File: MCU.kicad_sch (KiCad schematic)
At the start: 16 parts, among them J2 FTDI, SW1 SW_MEC_5G, SW2 SW_MEC_5G, U1 ESP32-WROOM-32, U2 AMS1117-3.3

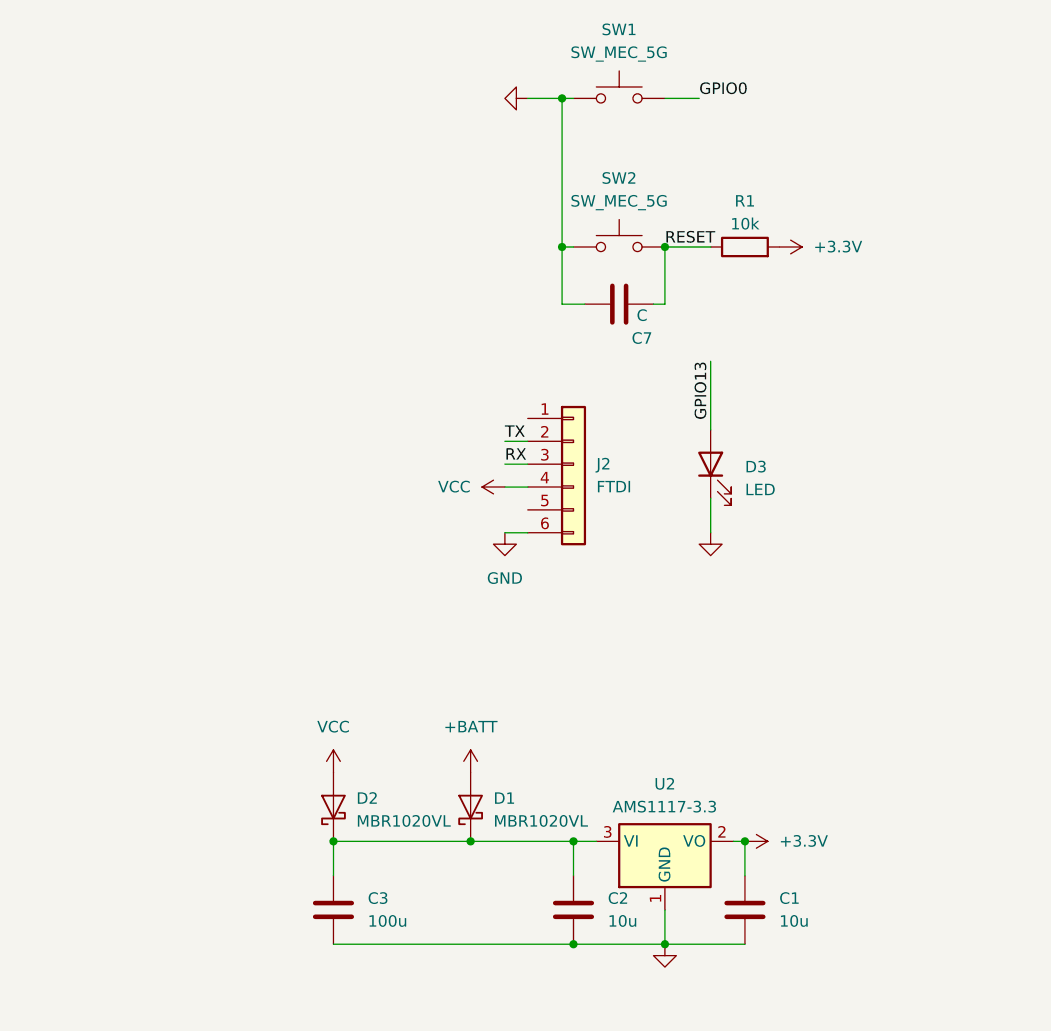
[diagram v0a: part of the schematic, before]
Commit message: Power Section done + added backup lipo
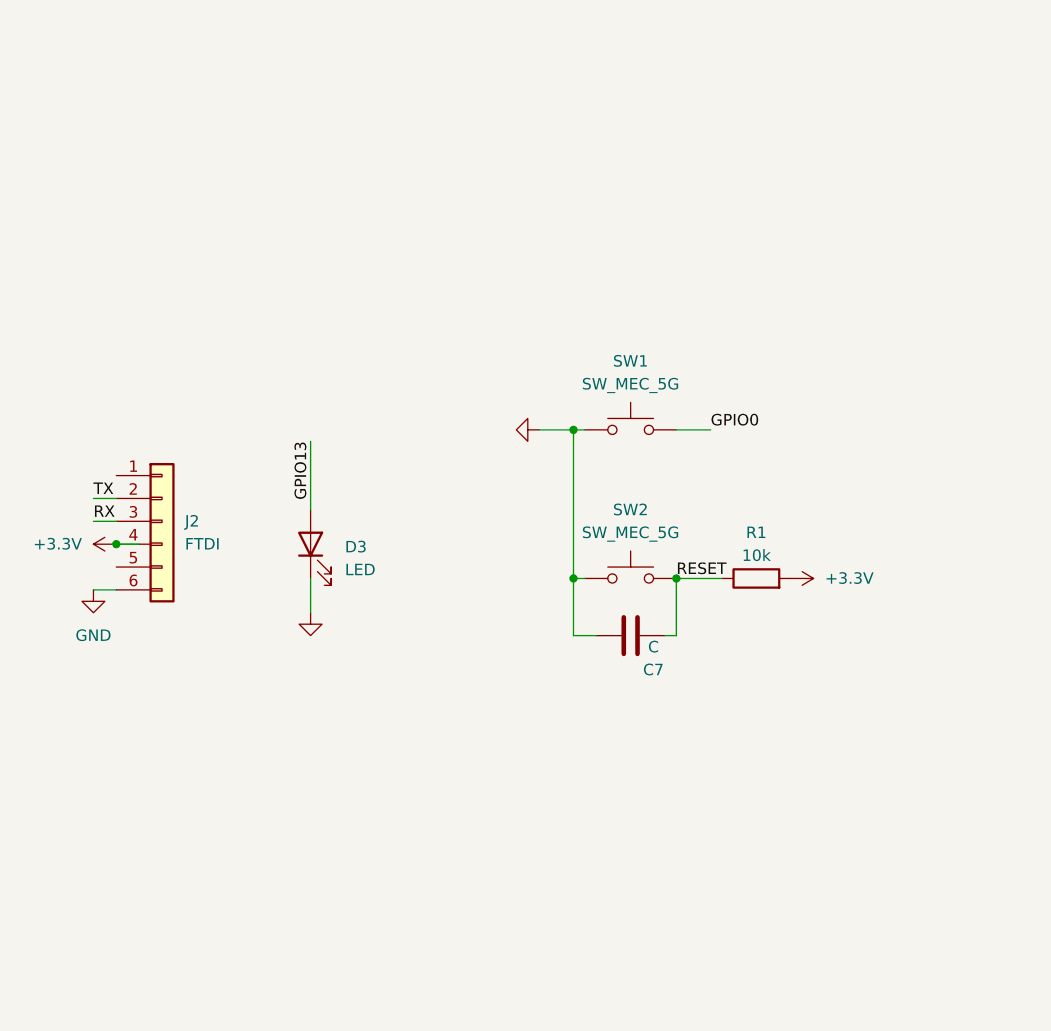
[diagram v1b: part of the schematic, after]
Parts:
- removed C1, C2: 10u, symbol Device:C
- removed C3: 100u, symbol Device:C
- removed D1, D2: MBR1020VL, Diode_SMD:D_SOD-123F, symbol Diode:MBR1020VL
- removed U2: AMS1117-3.3, Package_TO_SOT_SMD:SOT-223-3_TabPin2, symbol Regulator_Linear:AMS1117-3.3
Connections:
- net VCC is gone; now on net +3.3V: J2.4 (Pin_4)
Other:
- moved on the sheet: C7, D3, J2, R1, SW1, SW2

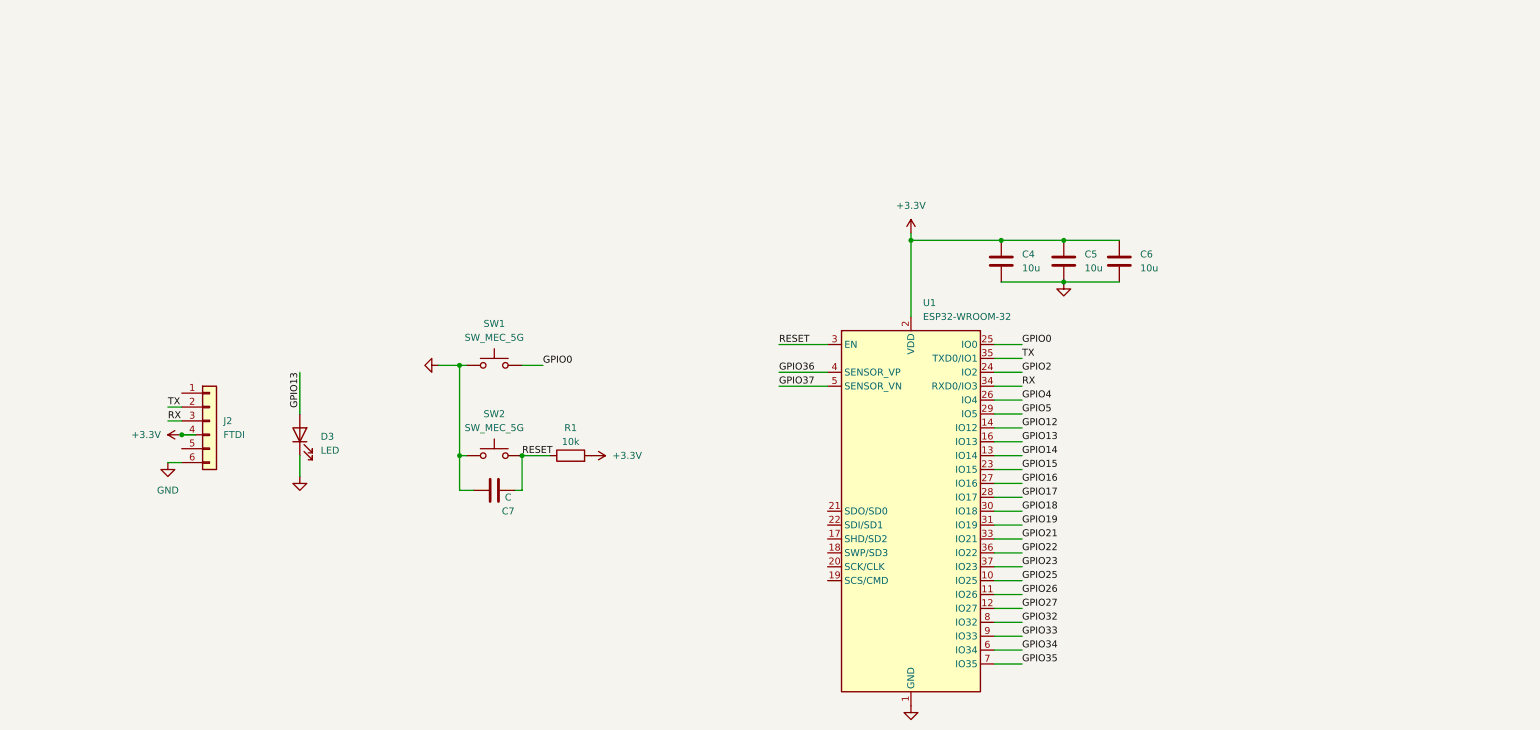
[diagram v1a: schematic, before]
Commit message: added io expander + rtc + fuel guage
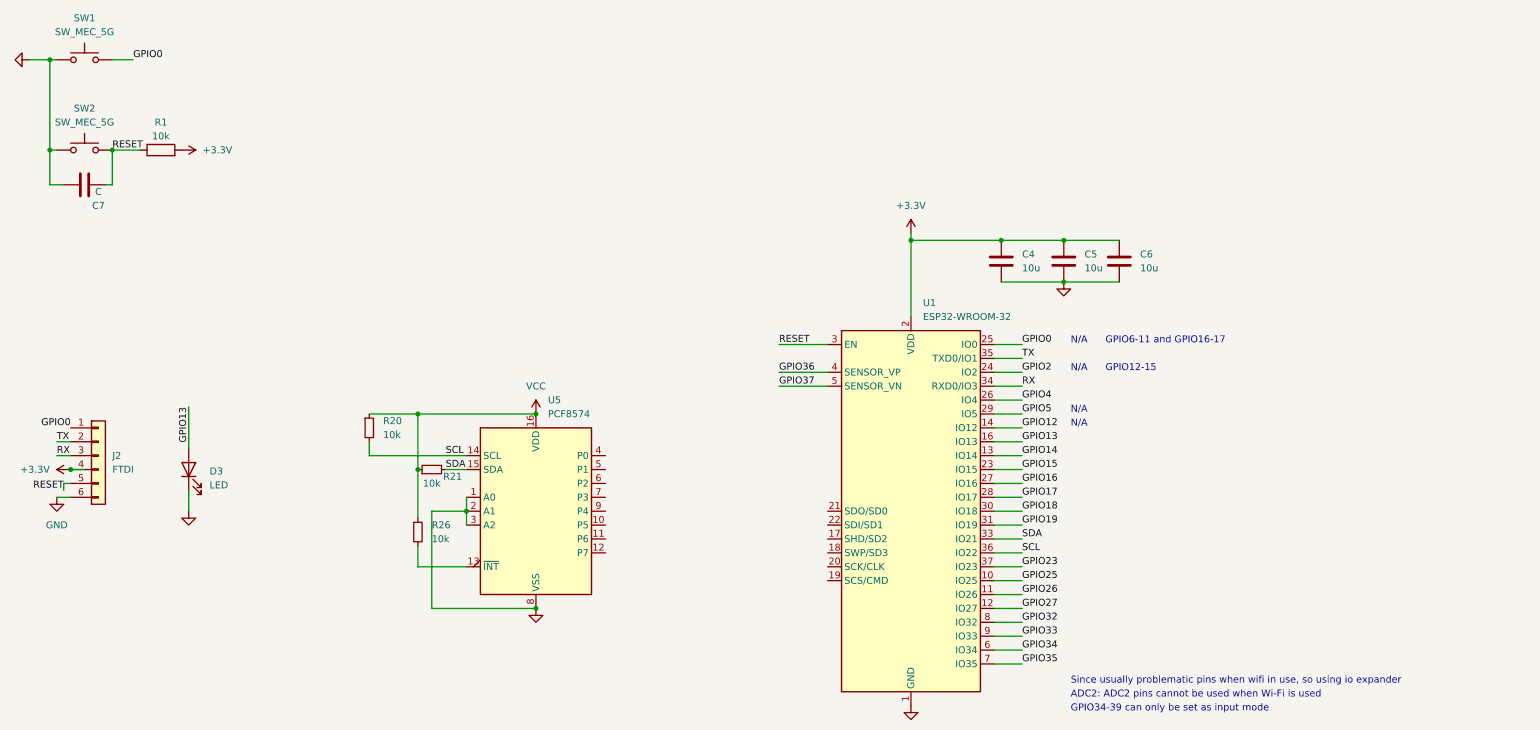
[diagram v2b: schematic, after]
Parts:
- added R20, R21, R26: 10k, symbol Device:R_Small
- added U5: PCF8574, symbol Interface_Expansion:PCF8574
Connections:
- net GND: now also U5.1 (A0), U5.2 (A1), U5.3 (A2), U5.8 (VSS)
- net GPIO0: now also J2.1 (Pin_1)
- net RESET: now also J2.5 (Pin_5)
- net GPIO21 renamed SDA
- net SDA: now also R21.2, U5.15 (SDA)
- net GPIO22 renamed SCL
- net SCL: now also R20.2, U5.14 (SCL)
- new net: R26.2, U5.13 (~{INT})
- new net VCC: R20.1, R21.1, R26.1, U5.16 (VDD)
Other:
- note added: "ADC2: ADC2 pins cannot be used when Wi-Fi is used"
- note added: "GPIO12-15"
- note added: "GPIO34-39 can only be set as input mode"
- note added: "GPIO6-11 and GPIO16-17"
- note added: "N/A"
- note added: "Since usually problematic pins when wifi in use, so using io expander"
- moved on the sheet: C7, D3, J2, R1, SW1, SW2

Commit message: Schematic Completed
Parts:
- removed D3: LED, symbol Device:LED
- added BT1: CR1220, symbol Device:Battery_Cell
- added C10: 10U, symbol Device:C
- added C11, C12: 6p, symbol Device:C_Small
- added C4: C_Small, symbol Device:C_Small
- added C9: 0.1U, symbol Device:C
- added R3, R4: 10k, symbol Device:R
- added R33, R34: 10k, symbol Device:R_Small
- added U3: DS3231M, Package_SO:SOIC-16W_7.5x10.3mm_P1.27mm, symbol Timer_RTC:DS3231M
- added U8: DS1307+, Package_DIP:DIP-8_W7.62mm, symbol Timer_RTC:DS1307+
- added Y1: 32.768kHz Quartz Crystal, symbol Device:Crystal_Small
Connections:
- net +3.3V: now also C10.1, C9.1, R3.1, R4.1, U3.2 (VCC)
- net GND: now also BT1.2 (-), C10.2, C4.1, C9.2, U3.10 (GND), U3.11 (GND), U3.12 (GND), U3.13 (GND), U3.5 (GND), U3.6 (GND), U3.7 (GND), U3.8 (GND), U3.9 (GND), U8.4 (GND)
- net SCL: now also R33.2, R4.2, U3.16 (SCL), U8.6 (SCL)
- net SDA: now also R3.2, R34.2, U3.15 (SDA), U8.5 (SDA)
- net VCC: now also C4.2, R33.1, R34.1, U8.3 (VBAT), U8.8 (VCC)
- net P_IO_4: now reaches U5.10 (P5)
- net P_IO_4: now also U5.9 (P4)
- net P_IO_5: now reaches U5.11 (P6)
- net P_IO_6: now reaches U5.12 (P7)
- net FAULT_LED: now reaches U5.4 (P0)
- net BUSY_LED: now reaches U5.5 (P1)
- net CON_LED: now reaches U5.6 (P2)
- net LED_PIN: now reaches U5.7 (P3)
- net GPIO13 renamed IO_LED
- net GPIO14 renamed MIST_PIN
- net GPIO15 renamed 12V_status
- net GPIO18 renamed TEMP1_DATA
- net GPIO19 renamed TEMP2_DATA
- net GPIO23 renamed BUZ_PIN
- net GPIO25 renamed WATER_PUMP_PIN
- net GPIO26 renamed FAN_EXHAUST_PIN
- net GPIO27 renamed turner
- net GPIO32 renamed heater
- net GPIO33 renamed ROTARY_DATA
- net GPIO34 renamed ROTARY_CLK
- net GPIO35 renamed ROT_SW
- net GPIO4 renamed FAN_CON_PIN
- net GPIO5 renamed WATER_LEVEL_DATA
- new net: BT1.1 (+), U3.14 (VBAT)
- new net: C11.1, C12.1
- new net: C12.2, U8.1 (X1), Y1.2
- new net: C11.2, U8.2 (X2), Y1.1
- new net 32KHZ: U3.1 (32KHZ)
- new net RTC_RESET: U3.4 (~{RST})
- new net SQW: U3.3 (~{INT}/SQW)
- no-connect marks 0 -> 6
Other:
- note added: "IE/OD"
- note added: "IO EXPANDER"
- note added: "MCU"
- note added: "OPTIONAL"
- note added: "PRIMARY"
- note added: "RTC"
- moved on the sheet: C4, C5, C6, C7, J2, R1, R20, R21, R26, SW1, SW2, U1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

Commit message: assigned footprints. another look needed. moving to pcb
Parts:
- removed BT1: CR1220, symbol Device:Battery_Cell
- removed C10: 10U, symbol Device:C
- removed C9: 0.1U, symbol Device:C
- removed R3, R4: 10k, symbol Device:R
- removed U3: DS3231M, Package_SO:SOIC-16W_7.5x10.3mm_P1.27mm, symbol Timer_RTC:DS3231M
- added BZ1: Buzzer, Buzzer_Beeper:Buzzer_12x9.5RM7.6, symbol Device:Buzzer
- added C1, C14: 0.1u, Capacitor_SMD:C_0402_1005Metric, symbol Device:C_Small
- added C13, C15, C17, C2, C8: 10u, Capacitor_SMD:C_0402_1005Metric, symbol Device:C_Small
- added C16: 10u, Capacitor_SMD:C_0805_2012Metric, symbol Device:C_Small
- added C18, C19, C21: 22u, Capacitor_SMD:C_0402_1005Metric, symbol Device:C_Small
- added C20: 10u, Capacitor_SMD:C_0402_1005Metric, symbol Device:C
- added D10, D11, D3, D6, D8: 1N4001, Diode_SMD:D_0805_2012Metric, symbol Diode:1N4001
- added D12: 1N5819, Diode_SMD:D_0805_2012Metric, symbol Diode:1N5819
- added D13, D14, D3: LED, LED_SMD:LED_0805_2012Metric, symbol Device:LED
- added D2: LED_PWR, LED_SMD:LED_0805_2012Metric, symbol Device:LED
- added D4: FAULT_LED, LED_SMD:LED_0805_2012Metric, symbol Device:LED
- added D5: BUSY_LED, Diode_SMD:D_0805_2012Metric, symbol Device:LED
- added D7: CONNECTIVITY_LED, LED_SMD:LED_0805_2012Metric, symbol Device:LED
- added F1: CAR_FUSE 2A, Fuse:Fuse_1206_3216Metric, symbol Device:Fuse
- added J10: mist, Connector_JST:JST_GH_SM02B-GHS-TB_1x02-1MP_P1.25mm_Horizontal, symbol Connector_Generic:Conn_01x02
- added J11: Led, LED_SMD:LED_0805_2012Metric, symbol Connector_Generic:Conn_01x02
- added J12: Water_Level, Connector_JST:JST_GH_SM03B-GHS-TB_1x03-1MP_P1.25mm_Horizontal, symbol Connector_Generic:Conn_01x03
- added J13: Main_Input_Jack, Connector_BarrelJack:BarrelJack_CLIFF_FC681465S_SMT_Horizontal, symbol Connector:Jack-DC
- added J14: Battery, Connector_JST:JST_EH_B2B-EH-A_1x02_P2.50mm_Vertical, symbol PCM_SL_Connectors:JST_02
- added J15: Display, Connector_JST:JST_GH_SM04B-GHS-TB_1x04-1MP_P1.25mm_Horizontal, symbol Connector_Generic:Conn_01x04
- added J16: Rotary_Encoder, Connector_JST:JST_GH_SM03B-GHS-TB_1x03-1MP_P1.25mm_Horizontal, symbol Connector_Generic:Conn_01x05
- added J17: Temp, Connector_JST:JST_GH_SM03B-GHS-TB_1x03-1MP_P1.25mm_Horizontal, symbol Connector_Generic:Conn_01x03
- added J18: Temp2, Connector_JST:JST_GH_SM03B-GHS-TB_1x03-1MP_P1.25mm_Horizontal, symbol Connector_Generic:Conn_01x03
- added J19: Water_Pump, Connector_JST:JST_GH_SM02B-GHS-TB_1x02-1MP_P1.25mm_Horizontal, symbol Connector_Generic:Conn_01x02
- added J20: Conn_01x04_Socket, Connector_JST:JST_GH_SM04B-GHS-TB_1x04-1MP_P1.25mm_Horizontal, symbol Connector:Conn_01x04_Socket
- added J21: extra, Connector_JST:JST_GH_SM06B-GHS-TB_1x06-1MP_P1.25mm_Horizontal, symbol Connector:Conn_01x06_Socket
- added J3, J4, J6: C8465, TerminalBlock:TerminalBlock_Altech_AK300-2_P5.00mm, symbol Connector:Screw_Terminal_01x02
- added J5, J7: Screw_Terminal_01x02, TerminalBlock:TerminalBlock_Altech_AK300-2_P5.00mm, symbol Connector:Screw_Terminal_01x02
- added J8: Fan_Exhaust, Connector_JST:JST_GH_SM02B-GHS-TB_1x02-1MP_P1.25mm_Horizontal, symbol Connector_Generic:Conn_01x02
- added J9: Fan_Continous, Connector_JST:JST_GH_SM02B-GHS-TB_1x02-1MP_P1.25mm_Horizontal, symbol Connector_Generic:Conn_01x02
- added JP1: Jumper_3_Bridged12, Jumper:SolderJumper-3_P1.3mm_Bridged2Bar12_Pad1.0x1.5mm_NumberLabels, symbol Jumper:Jumper_3_Bridged12
- added JP2: BUCK_BOOST_JUMP, Jumper:SolderJumper-2_P1.3mm_Bridged_RoundedPad1.0x1.5mm, symbol Jumper:Jumper_2_Bridged
- added JP3: Jumper_2_Open, Jumper:SolderJumper-2_P1.3mm_Open_Pad1.0x1.5mm, symbol Jumper:Jumper_2_Open
- added L1: 1.5u, Inductor_SMD:L_6.3x6.3_H3, symbol Device:L
- added Q10, Q2, Q3, Q4, Q5, Q6, Q8, Q9: AO3406, Package_TO_SOT_SMD:SOT-23, symbol Simulation_SPICE:NMOS
- added Q7: SI2301, Package_TO_SOT_SMD:SOT-23, symbol Transistor_FET:Si2319CDS
- added R10, R13, R35, R38, R39, R41: 10K, Resistor_SMD:R_0201_0603Metric, symbol Device:R
- added R11, R12, R14, R15: 1K, Resistor_SMD:R_0201_0603Metric, symbol Device:R
- added R16: 1.3k, Resistor_SMD:R_0201_0603Metric, symbol Device:R
- added R17, R18, R19, R22, R23, R24: 10k, Resistor_SMD:R_0201_0603Metric, symbol Device:R_Small
- added R25: 68.1k, Resistor_SMD:R_0201_0603Metric, symbol Device:R_Small
- added R27, R29: 10k, Resistor_SMD:R_0201_0603Metric, symbol Device:R
- added R28: 20k, Resistor_SMD:R_0201_0603Metric, symbol Device:R
- added R30: 213k, Resistor_SMD:R_0201_0603Metric, symbol Device:R_Small
- added R31, R32: 1.5k, Resistor_SMD:R_0201_0603Metric, symbol Device:R
- added R36, R37, R40: 1K, Resistor_SMD:R_0805_2012Metric, symbol Device:R
- added R5, R6: 330, Resistor_SMD:R_0201_0603Metric, symbol Device:R_Small
- added R8, R9: 1k, Resistor_SMD:R_0201_0603Metric, symbol Device:R_Small
- added SW4: SW, Button_Switch_SMD:Nidec_Copal_CAS-120A, symbol Switch:SW_Nidec_CAS-120A1
- added U1: ~, Package_DFN_QFN:TDFN-8-1EP_2x2mm_P0.5mm_EP0.8x1.2mm, symbol Custom:MAX17048
- added U10, U9: G5NB-1A-E DC12, Package_SIP:SIP4_Sharp-SSR_P7.62mm_Straight, symbol Relay_SolidState:S102S01
- added U4: ~, Package_DFN_QFN:TDFN-8-1EP_2x2mm_P0.5mm_EP0.8x1.2mm, symbol Custom:TPS63070
- added U4: TP4056, TP4056:SOP127P600X175-9N, symbol Custom:TP4056
- added U6: LM7805_TO220, Package_TO_SOT_THT:TO-220F-3_Horizontal_TabDown, symbol Regulator_Linear:LM7805_TO220
- C12: renamed from C4; footprint (none) -> Capacitor_SMD:C_0402_1005Metric
- C4: renamed from C12; footprint (none) -> Capacitor_SMD:C_0402_1005Metric
- C4, C5, C6: footprint (none) -> Capacitor_SMD:C_0402_1005Metric
- C7: value C -> 0.1u; footprint (none) -> Capacitor_SMD:C_0402_1005Metric
- C9: renamed from C11; footprint (none) -> Capacitor_SMD:C_0402_1005Metric
- J2: footprint (none) -> Connector_PinHeader_2.54mm:PinHeader_1x06_P2.54mm_Horizontal
- R1, R20, R21, R26: footprint (none) -> Resistor_SMD:R_0201_0603Metric
- R3: renamed from R34; footprint (none) -> Resistor_SMD:R_0201_0603Metric
- R4: renamed from R33; footprint (none) -> Resistor_SMD:R_0201_0603Metric
- SW1, SW2: footprint (none) -> Button_Switch_SMD:SW_SPST_B3U-1000P
- U5: footprint (none) -> PCF8574T_3_518:SOIC127P1032X265-16N
- Y1: footprint (none) -> Crystal:Crystal_SMD_3215-2Pin_3.2x1.5mm
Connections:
- net VCC is gone; now on net +3.3V: C12.2, R20.1, R21.1, R26.1, R3.1, R4.1, U5.16 (VDD), U8.3 (VBAT), U8.8 (VCC)
- net +3.3V: now also C17.1, C18.1, C19.1, C21.1, J12.2 (Pin_2), J15.2 (Pin_2), J16.2 (Pin_2), J17.2 (Pin_2), J18.2 (Pin_2), JP1.3 (B), JP3.2 (B), R18.1, R19.1, R22.1, R30.1, R31.1, R32.2, U4.7 (VOUT), U4.8 (VOUT)
- net 12V_status: now also R27.2, R28.1
- net BUSY_LED: now also D5.2 (A)
- net BUZ_PIN: now also Q9.2 (G), R39.2
- net CON_LED: now also D7.2 (A)
- net FAN_CON_PIN: now also Q5.2 (G), R13.2
- net FAN_EXHAUST_PIN: now also Q4.2 (G), R10.2
- net FAULT_LED: now also D4.2 (A)
- net GND: now also C1.2, C13.2, C14.2, C15.2, C16.2, C17.2, C18.2, C19.2, C2.2, C20.2, C21.2, C8.2, J12.1 (Pin_1), J13.2, J14.1, J15.1 (Pin_1), J16.1 (Pin_1), J17.1 (Pin_1), J18.1 (Pin_1), Q10.3 (S), Q4.3 (S), Q5.3 (S), Q6.3 (S), Q8.3 (S), Q9.3 (S), R10.1, R11.2, R12.2, R13.1, R14.2, R15.2, R16.2, R17.2, R25.2, R28.2, R29.2, R35.1, R37.2, R38.1, R39.1, R41.1, R5.2, R6.2, R8.2, R9.2, U1.1 (VSS), U4.1 (Temp1), U4.10 (PGND), U4.15 (VSEL), U4.2 (PG), U4.3 (GND), U4.4 (GND), U4.6 (FB2), U6.2 (GND)
- net GPIO12: now also J21.5 (Pin_5)
- net GPIO16: now also J21.4 (Pin_4)
- net GPIO17: now also J21.3 (Pin_3)
- net GPIO2: now also J21.6 (Pin_6)
- net GPIO36: now also J21.2 (Pin_2)
- net GPIO37: now also J21.1 (Pin_1)
- net IO_LED: now also D3.2 (A)
- net LED_PIN: now also Q8.2 (G), R38.2
- net MIST_PIN: now also Q6.2 (G), R35.2
- net P_IO_4: now also J20.3 (Pin_3), J20.4 (Pin_4)
- net P_IO_5: now also J20.2 (Pin_2)
- net P_IO_6: now also J20.1 (Pin_1)
- net ROTARY_CLK: now also J16.4 (Pin_4)
- net ROTARY_DATA: now also J16.5 (Pin_5)
- net ROT_SW: now also J16.3 (Pin_3)
- net SCL: now also J15.4 (Pin_4), R19.2, U1.7 (SCL)
- net SDA: now also J15.3 (Pin_3), JP3.1 (A), R18.2, U1.8 (SDA)
- net TEMP1_DATA: now also J17.3 (Pin_3)
- net TEMP2_DATA: now also J18.3 (Pin_3)
- net WATER_LEVEL_DATA: now also J12.3 (Pin_3)
- net WATER_PUMP_PIN: now also Q10.2 (G), R41.2
- net heater: now also Q2.2 (G), R5.1
- net turner: now also Q3.2 (G), R6.1
- new net: J4.1 (Pin_1), J4.2 (Pin_2), J5.1 (Pin_1), J5.2 (Pin_2), U10.2
- new net: J14.2, SW4.2 (B)
- new net: D8.2 (A), Q6.1 (D), R36.1
- new net: F1.1, J13.1
- new net: D7.1 (K), R15.1
- new net: D6.2 (A), J9.2 (Pin_2), Q5.1 (D)
- new net: J6.1 (Pin_1), J6.2 (Pin_2), J7.1 (Pin_1), J7.2 (Pin_2), U10.1
- new net: Q2.1 (D), U10.4
- new net: L1.1, U4.11 (L1)
- new net: C1.1, C13.1, C2.1, C8.1, JP2.2 (B), R23.1, R24.1, U4.12 (VIN), U4.13 (VIN)
- new net: C14.1, U4.3 (VAUX)
- new net: R25.1, R30.2, U4.5 (FB)
- new net: L1.2, U4.9 (L2)
- new net: R22.2, U1.5 (ALERT)
- new net: D13.1 (K), U4.7 (CHRG)
- new net: D13.2 (A), R31.2
- new net: D4.1 (K), R12.1
- new net: R29.1, U4.2 (PROG)
- new net: D14.1 (K), U4.6 (STDBY)
- new net: J11.2 (Pin_2), Q8.1 (D)
- new net: D3.2 (A), J8.2 (Pin_2), Q4.1 (D)
- new net: D11.2 (A), J19.2 (Pin_2), Q10.1 (D)
- new net: Q9.1 (D), R40.2
- new net: J10.2 (Pin_2), R36.2
- new net: Q3.1 (D), U9.4
- new net: Q3.3 (S), R9.1
- new net: R17.1, U1.6 (QSTART)
- new net: D14.2 (A), R32.1
- new net: Q2.3 (S), R8.1
- new net: BZ1.2 (+), D10.2 (A), R40.1
- new net: JP1.2 (C), U1.3 (VDD)
- new net: D5.1 (K), R14.1
- new net: J3.1 (Pin_1), U9.2
- new net: J3.2 (Pin_2), U9.1
- new net: D2.1 (K), R11.1
- new net: D3.1 (K), R37.1
- new net +12V: BZ1.1 (-), C15.1, D10.1 (K), D11.1 (K), D12.2 (A), D2.2 (A), D3.1 (K), D6.1 (K), D8.1 (K), F1.2, J10.1 (Pin_1), J11.1 (Pin_1), J19.1 (Pin_1), J8.1 (Pin_1), J9.1 (Pin_1), Q7.1 (G), R16.1, U10.3, U6.1 (VI), U9.3
- new net +5V: C16.1, C20.1, R27.1, U4.4 (VCC), U4.8 (CE), U6.3 (VO)
- new net Buck_In: D12.1 (K), JP2.1 (A), Q7.2 (S)
- new net EN: R23.2, U4.14 (EN)
- new net MCU_BAT: JP1.1 (A), Q7.3 (D), SW4.1 (C), U1.2 (CELL), U4.5 (BAT)
- new net PS: R24.2, U4.1 (PSYNC)
- no-connect marks 6 -> 8
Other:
- note added: "BMS"
- note added: "BUCK-BOOST -> 3.3V"
- note added: "Battery Monitor"
- note added: "HEATER"
- note added: "Input"
- note added: "JST connectors"
- note added: "LEDS"
- note added: "Need this to have vbat as reference voltage. things get complicated otherwise I think so"
- note added: "Outputs"
- note added: "Power Selector"
- note added: "Power Selector Incase of both plugged in"
- note added: "Primary AC"
- note added: "R(SET) = 68.1 * (VOUT/0.8-1)"
- note added: "SET AT 3.3V"
- note added: "Screw terminal"
- note added: "Sensors/Inputs"
- note added: "TURNER"
- note added: "Using this because i have buck boost regulator. usually it's a problem with that."
- note added: "low rds onn and low gate(th)"
- note added: "small 1 cell 3.7V LiPo battery"
- note added: "ssr relay"
- note added: "tps63070"
- note removed: "OPTIONAL"
